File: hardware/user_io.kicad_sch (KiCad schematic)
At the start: 6 parts

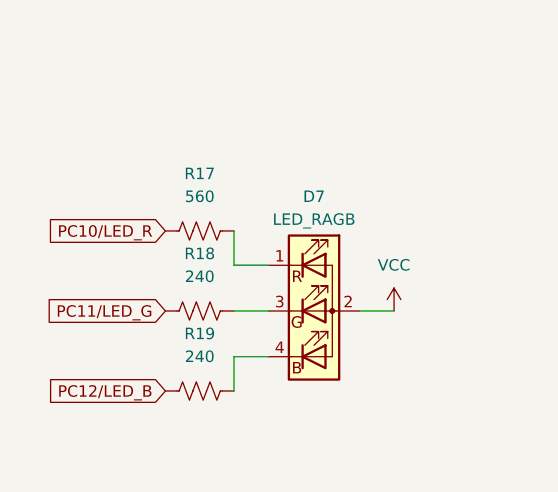
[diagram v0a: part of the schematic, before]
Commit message: wip: schematic fixes based on testing
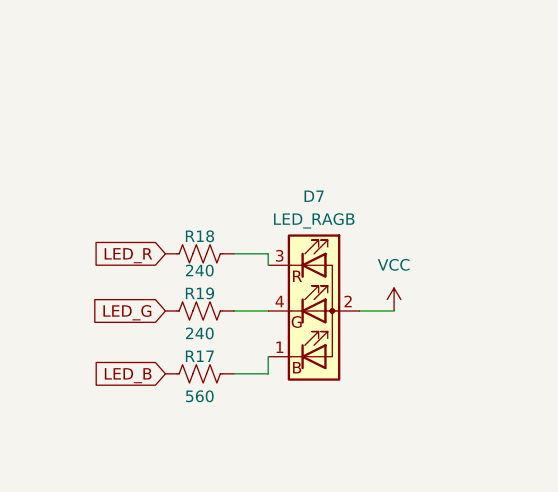
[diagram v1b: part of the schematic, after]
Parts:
- D7: symbol Device:LED_RAGB -> Device:LED_BARG
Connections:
- net PC10/LED_R renamed LED_B
- net PC11/LED_G renamed LED_R
- net PC12/LED_B renamed LED_G
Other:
- moved on the sheet: R17, R18, R19
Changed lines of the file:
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@@
   (title_block
     (title "DSP PAW add-on board")
-    (date "2023-08-19")
+    (date "2023-09-04")
+    (rev "2")
     (company "bitgloo")
     (comment 1 "Released under the CERN Open Hardware Licence Version 2 - Strongly Reciprocal")
   )
+  (wire (pts (xy 96.52 113.665) (xy 100.33 113.665))
+    (stroke (width 0) (type default))
+  )
+  (wire (pts (xy 110.49 106.68) (xy 114.3 106.68))
+    (stroke (width 0) (type default))
+  )
   (wire (pts (xy 96.52 106.68) (xy 100.33 106.68))
     (stroke (width 0) (type default))
   )
-  (wire (pts (xy 96.52 111.76) (xy 100.33 111.76))
-    (stroke (width 0) (type default))
-  )
-  (wire (pts (xy 110.49 106.68) (xy 114.3 106.68))
-    (stroke (width 0) (type default))
-  )
-  (wire (pts (xy 96.52 115.57) (xy 96.52 111.76))
-    (stroke (width 0) (type default))
-  )
-  (wire (pts (xy 96.52 97.79) (xy 96.52 101.6))
-    (stroke (width 0) (type default))
-  )
-  (wire (pts (xy 96.52 101.6) (xy 100.33 101.6))
+  (wire (pts (xy 100.33 113.665) (xy 100.33 111.76))
+    (stroke (width 0) (type default))
+  )
+  (wire (pts (xy 96.52 100.33) (xy 100.33 100.33))
+    (stroke (width 0) (type default))
+  )
+  (wire (pts (xy 100.33 100.33) (xy 100.33 101.6))
     (stroke (width 0) (type default))
   )
@@
     )
   )
-  (global_label "PC12{slash}LED_B" (shape input) (at 88.9 115.57 180) (fields_autoplaced)
+  (global_label "LED_G" (shape input) (at 88.9 106.68 180) (fields_autoplaced)
     (effects (font (size 1.27 1.27)) (justify right))
-    (property "Intersheetrefs" "${INTERSHEET_REFS}" (at 74.5126 115.4906 0)
+    (property "Intersheetrefs" "${INTERSHEET_REFS}" (at 80.3095 106.68 0)
       (effects (font (size 1.27 1.27)) (justify right) hide)
     )
   )
-  (global_label "PC10{slash}LED_R" (shape input) (at 88.9 97.79 180) (fields_autoplaced)
+  (global_label "LED_B" (shape input) (at 88.9 113.665 180) (fields_autoplaced)
     (effects (font (size 1.27 1.27)) (justify right))
-    (property "Intersheetrefs" "${INTERSHEET_REFS}" (at 74.5126 97.7106 0)
+    (property "Intersheetrefs" "${INTERSHEET_REFS}" (at 80.3095 113.665 0)
       (effects (font (size 1.27 1.27)) (justify right) hide)
     )
@@
     )
   )
-  (global_label "PC11{slash}LED_G" (shape input) (at 88.9 106.68 180) (fields_autoplaced)
+  (global_label "LED_R" (shape input) (at 88.9 100.33 180) (fields_autoplaced)
     (effects (font (size 1.27 1.27)) (justify right))
-    (property "Intersheetrefs" "${INTERSHEET_REFS}" (at 74.5126 106.6006 0)
+    (property "Intersheetrefs" "${INTERSHEET_REFS}" (at 80.3095 100.33 0)
       (effects (font (size 1.27 1.27)) (justify right) hide)
     )
@@
     )
   )
-  (symbol (lib_id "Device:R_US") (at 92.71 106.68 90) (unit 1)
-    (in_bom yes) (on_board yes) (dnp no) (fields_autoplaced)
-    (property "Reference" "R18" (at 92.71 100.33 90)
-      (effects (font (size 1.27 1.27)))
-    )
-    (property "Value" "240" (at 92.71 102.87 90)
-      (effects (font (size 1.27 1.27)))
-    )
-    (property "Footprint" "Resistor_SMD:R_0603_1608Metric" (at 92.964 105.664 90)
-      (effects (font (size 1.27 1.27)) hide)
-    )
-    (property "Datasheet" "" (at 92.71 106.68 0)
-      (effects (font (size 1.27 1.27)) hide)
-    )
-    (property "Part Number" "RC0603JR-07240RL" (at 92.71 106.68 0)
-      (effects (font (size 1.27 1.27)) hide)
-    )
-    (property "DNP" "" (at 92.71 106.68 0)
-      (effects (font (size 1.27 1.27)) hide)
-    )
-    (property "LCSC Part #" "C23350" (at 92.71 106.68 0)
+  (symbol (lib_id "Device:R_US") (at 92.71 100.33 90) (unit 1)
+    (in_bom yes) (on_board yes) (dnp no)
+    (property "Reference" "R18" (at 92.71 98.425 90)
+      (effects (font (size 1.27 1.27)))
+    )
+    (property "Value" "240" (at 92.71 102.235 90)
+      (effects (font (size 1.27 1.27)))
+    )
+    (property "Footprint" "Resistor_SMD:R_0603_1608Metric" (at 92.964 99.314 90)
+      (effects (font (size 1.27 1.27)) hide)
+    )
+    (property "Datasheet" "" (at 92.71 100.33 0)
+      (effects (font (size 1.27 1.27)) hide)
+    )
+    (property "Part Number" "RC0603JR-07240RL" (at 92.71 100.33 0)
+      (effects (font (size 1.27 1.27)) hide)
+    )
+    (property "DNP" "" (at 92.71 100.33 0)
+      (effects (font (size 1.27 1.27)) hide)
+    )
+    (property "LCSC Part #" "C23350" (at 92.71 100.33 0)
       (effects (font (size 1.27 1.27)) hide)
     )
@@
     )
   )
-  (symbol (lib_id "Device:R_US") (at 92.71 97.79 90) (unit 1)
-    (in_bom yes) (on_board yes) (dnp no) (fields_autoplaced)
-    (property "Reference" "R17" (at 92.71 91.44 90)
-      (effects (font (size 1.27 1.27)))
-    )
-    (property "Value" "560" (at 92.71 93.98 90)
-      (effects (font (size 1.27 1.27)))
-    )
-    (property "Footprint" "Resistor_SMD:R_0603_1608Metric" (at 92.964 96.774 90)
-      (effects (font (size 1.27 1.27)) hide)
-    )
-    (property "Datasheet" "" (at 92.71 97.79 0)
-      (effects (font (size 1.27 1.27)) hide)
-    )
-    (property "Part Number" "RC0603JR-07560RL" (at 92.71 97.79 0)
-      (effects (font (size 1.27 1.27)) hide)
-    )
-    (property "DNP" "" (at 92.71 97.79 0)
-      (effects (font (size 1.27 1.27)) hide)
-    )
-    (property "LCSC Part #" "C23204" (at 92.71 97.79 0)
+  (symbol (lib_id "Device:R_US") (at 92.71 113.665 90) (unit 1)
+    (in_bom yes) (on_board yes) (dnp no)
+    (property "Reference" "R17" (at 92.71 111.76 90)
+      (effects (font (size 1.27 1.27)))
+    )
+    (property "Value" "560" (at 92.71 116.205 90)
+      (effects (font (size 1.27 1.27)))
+    )
+    (property "Footprint" "Resistor_SMD:R_0603_1608Metric" (at 92.964 112.649 90)
+      (effects (font (size 1.27 1.27)) hide)
+    )
+    (property "Datasheet" "" (at 92.71 113.665 0)
+      (effects (font (size 1.27 1.27)) hide)
+    )
+    (property "Part Number" "RC0603JR-07560RL" (at 92.71 113.665 0)
+      (effects (font (size 1.27 1.27)) hide)
+    )
+    (property "DNP" "" (at 92.71 113.665 0)
+      (effects (font (size 1.27 1.27)) hide)
+    )
+    (property "LCSC Part #" "C23204" (at 92.71 113.665 0)
       (effects (font (size 1.27 1.27)) hide)
     )
@@
     )
   )
-  (symbol (lib_id "Device:LED_RAGB") (at 105.41 106.68 0) (unit 1)
+  (symbol (lib_id "Device:LED_BARG") (at 105.41 106.68 0) (unit 1)
     (in_bom yes) (on_board yes) (dnp no) (fields_autoplaced)
     (property "Reference" "D7" (at 105.41 93.98 0)
@@
     )
   )
-  (symbol (lib_id "Device:R_US") (at 92.71 115.57 90) (unit 1)
-    (in_bom yes) (on_board yes) (dnp no) (fields_autoplaced)
-    (property "Reference" "R19" (at 92.71 109.22 90)
-      (effects (font (size 1.27 1.27)))
-    )
-    (property "Value" "240" (at 92.71 111.76 90)
-      (effects (font (size 1.27 1.27)))
-    )
-    (property "Footprint" "Resistor_SMD:R_0603_1608Metric" (at 92.964 114.554 90)
-      (effects (font (size 1.27 1.27)) hide)
-    )
-    (property "Datasheet" "" (at 92.71 115.57 0)
-      (effects (font (size 1.27 1.27)) hide)
-    )
-    (property "Part Number" "RC0603JR-07240RL" (at 92.71 115.57 0)
-      (effects (font (size 1.27 1.27)) hide)
-    )
-    (property "DNP" "" (at 92.71 115.57 0)
-      (effects (font (size 1.27 1.27)) hide)
-    )
-    (property "LCSC Part #" "C23350" (at 92.71 115.57 0)
-      (effects (font (size 1.27 1.27)) hide)
-    )
+  (symbol (lib_id "Device:R_US") (at 92.71 106.68 90) (unit 1)
+    (in_bom yes) (on_board yes) (dnp no)
+    (property "Reference" "R19" (at 92.71 104.775 90)
+      (effects (font (size 1.27 1.27)))
+    )
+    (property "Value" "240" (at 92.71 109.22 90)
+      (effects (font (size 1.27 1.27)))
+    )
+    (property "Footprint" "Resistor_SMD:R_0603_1608Metric" (at 92.964 105.664 90)
+      (effects (font (size 1.27 1.27)) hide)
+    )
+    (property "Datasheet" "" (at 92.71 106.68 0)
+      (effects (font (size 1.27 1.27)) hide)
+    )
+    (property "Part Number" "RC0603JR-07240RL" (at 92.71 106.68 0)
+      (effects (font (size 1.27 1.27)) hide)
+    )
+    (property "DNP" "" (at 92.71 106.68 0)
+      (effects (font (size 1.27 1.27)) hide)
+    )
+    (property "LCSC Part #" "C23350" (at 92.71 106.68 0)
+      (effects (font (size 1.27 1.27)) hide)
+    )

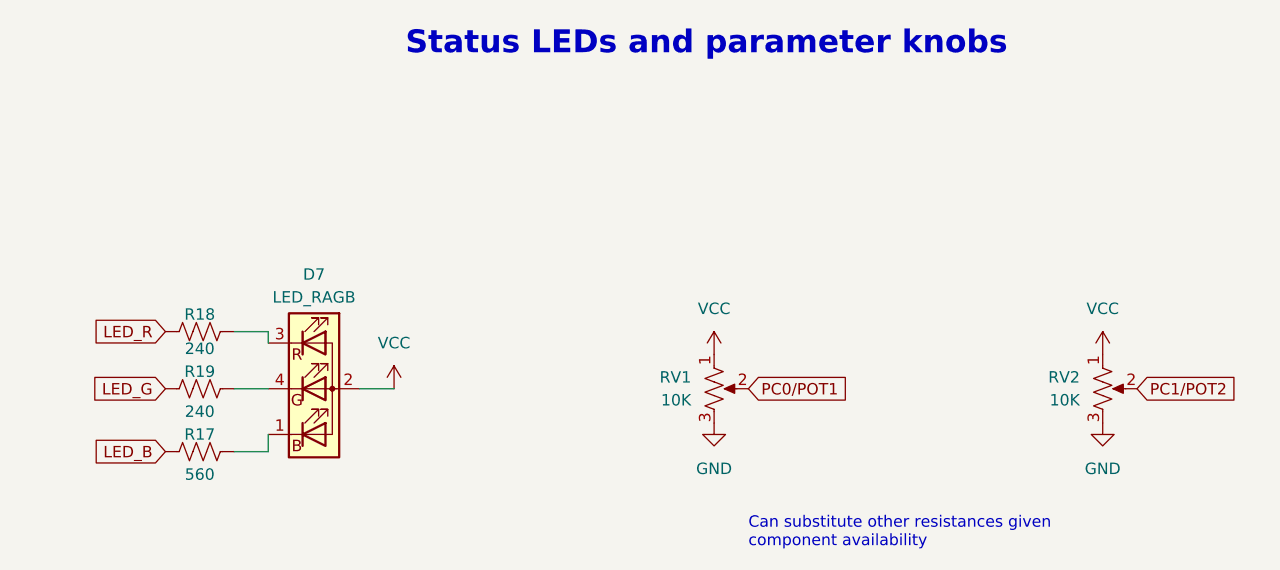
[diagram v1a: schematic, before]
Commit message: vdda buffer; vdda for pots; other fixes
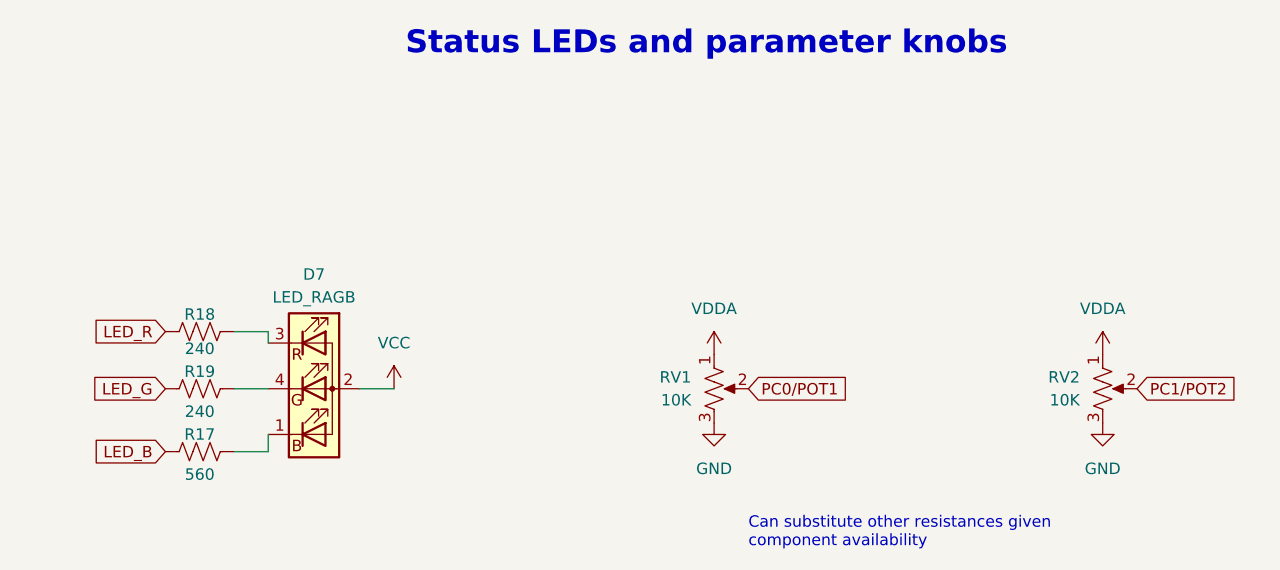
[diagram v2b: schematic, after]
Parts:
- D7: LCSC Part # C427425 -> (none)
- R17: LCSC Part # C23204 -> (none)
- R18, R19: LCSC Part # C23350 -> (none)
- RV1, RV2: LCSC Part # C330458 -> (none)
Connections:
- net VCC: no longer RV1.1, RV2.1
- new net VDDA: RV1.1, RV2.1
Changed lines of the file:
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@@
-      (effects (font (size 1.27 1.27)) hide)
-    )
-    (property "LCSC Part #" "C330458" (at 193.04 106.68 0)
       (effects (font (size 1.27 1.27)) hide)
     )
@@
         (path "/c291319b-d76e-4fda-91cc-061acff65f9f/7798c5d5-f9b1-4b2e-811c-a15abcd34bfa"
           (reference "RV2") (unit 1)
-        )
-      )
-    )
-  )
-  (symbol (lib_id "power:VCC") (at 193.04 102.87 0) (unit 1)
-    (in_bom yes) (on_board yes) (dnp no) (fields_autoplaced)
-    (property "Reference" "#PWR056" (at 193.04 106.68 0)
-      (effects (font (size 1.27 1.27)) hide)
-    )
-    (property "Value" "VCC" (at 193.04 97.79 0)
-      (effects (font (size 1.27 1.27)))
-    )
-    (property "Footprint" "" (at 193.04 102.87 0)
-      (effects (font (size 1.27 1.27)) hide)
-    )
-    (property "Datasheet" "" (at 193.04 102.87 0)
-      (effects (font (size 1.27 1.27)) hide)
-    )
-    (pin "1")
-    (instances
-      (project "stmdsp_rev3"
-        (path "/975c3983-57e7-4e06-a697-831e5209dd80"
-          (reference "#PWR056") (unit 1)
-        )
-      )
-      (project "DSP PAW add-on board"
-        (path "/c291319b-d76e-4fda-91cc-061acff65f9f/270d19d2-3af2-41db-ad1c-33373417ec82"
-          (reference "#PWR027") (unit 1)
-        )
-        (path "/c291319b-d76e-4fda-91cc-061acff65f9f/7798c5d5-f9b1-4b2e-811c-a15abcd34bfa"
-          (reference "#PWR068") (unit 1)
         )
       )
@@
       (effects (font (size 1.27 1.27)) hide)
     )
-    (property "LCSC Part #" "C23350" (at 92.71 100.33 0)
-      (effects (font (size 1.27 1.27)) hide)
-    )
     (pin "1")
     (pin "2")
@@
         (path "/c291319b-d76e-4fda-91cc-061acff65f9f/7798c5d5-f9b1-4b2e-811c-a15abcd34bfa"
           (reference "#PWR070") (unit 1)
+        )
+      )
+    )
+  )
+  (symbol (lib_id "power:VDDA") (at 193.04 102.87 0) (unit 1)
+    (in_bom yes) (on_board yes) (dnp no) (fields_autoplaced)
+    (property "Reference" "#PWR013" (at 193.04 106.68 0)
+      (effects (font (size 1.27 1.27)) hide)
+    )
+    (property "Value" "VDDA" (at 193.04 97.79 0)
+      (effects (font (size 1.27 1.27)))
+    )
+    (property "Footprint" "" (at 193.04 102.87 0)
+      (effects (font (size 1.27 1.27)) hide)
+    )
+    (property "Datasheet" "" (at 193.04 102.87 0)
+      (effects (font (size 1.27 1.27)) hide)
+    )
+    (pin "1")
+    (instances
+      (project "stmdsp_rev3"
+        (path "/975c3983-57e7-4e06-a697-831e5209dd80"
+          (reference "#PWR013") (unit 1)
+        )
+      )
+      (project "DSP PAW add-on board"
+        (path "/c291319b-d76e-4fda-91cc-061acff65f9f/270d19d2-3af2-41db-ad1c-33373417ec82"
+          (reference "#PWR033") (unit 1)
+        )
+        (path "/c291319b-d76e-4fda-91cc-061acff65f9f/97fc232a-dbc7-49da-a6a0-e33e9aacbabd"
+          (reference "#PWR024") (unit 1)
+        )
+        (path "/c291319b-d76e-4fda-91cc-061acff65f9f/7798c5d5-f9b1-4b2e-811c-a15abcd34bfa"
+          (reference "#PWR067") (unit 1)
         )
       )
@@
       (effects (font (size 1.27 1.27)) hide)
     )
-    (property "LCSC Part #" "C23204" (at 92.71 113.665 0)
-      (effects (font (size 1.27 1.27)) hide)
-    )
     (pin "1")
     (pin "2")
@@
     )
   )
-  (symbol (lib_id "power:VCC") (at 149.86 102.87 0) (unit 1)
-    (in_bom yes) (on_board yes) (dnp no) (fields_autoplaced)
-    (property "Reference" "#PWR055" (at 149.86 106.68 0)
-      (effects (font (size 1.27 1.27)) hide)
-    )
-    (property "Value" "VCC" (at 149.86 97.79 0)
-      (effects (font (size 1.27 1.27)))
-    )
-    (property "Footprint" "" (at 149.86 102.87 0)
-      (effects (font (size 1.27 1.27)) hide)
-    )
-    (property "Datasheet" "" (at 149.86 102.87 0)
-      (effects (font (size 1.27 1.27)) hide)
-    )
-    (pin "1")
-    (instances
-      (project "stmdsp_rev3"
-        (path "/975c3983-57e7-4e06-a697-831e5209dd80"
-          (reference "#PWR055") (unit 1)
-        )
-      )
-      (project "DSP PAW add-on board"
-        (path "/c291319b-d76e-4fda-91cc-061acff65f9f/270d19d2-3af2-41db-ad1c-33373417ec82"
-          (reference "#PWR023") (unit 1)
-        )
-        (path "/c291319b-d76e-4fda-91cc-061acff65f9f/7798c5d5-f9b1-4b2e-811c-a15abcd34bfa"
-          (reference "#PWR067") (unit 1)
-        )
-      )
-    )
-  )
   (symbol (lib_id "Device:LED_BARG") (at 105.41 106.68 0) (unit 1)
     (in_bom yes) (on_board yes) (dnp no) (fields_autoplaced)
@@
     )
     (property "DNP" "" (at 105.41 106.68 0)
-      (effects (font (size 1.27 1.27)) hide)
-    )
-    (property "LCSC Part #" "C427425" (at 105.41 106.68 0)
       (effects (font (size 1.27 1.27)) hide)
     )
@@
       (effects (font (size 1.27 1.27)) hide)
     )
-    (property "LCSC Part #" "C23350" (at 92.71 106.68 0)
-      (effects (font (size 1.27 1.27)) hide)
-    )
     (pin "1")
     (pin "2")
@@
         (path "/c291319b-d76e-4fda-91cc-061acff65f9f/7798c5d5-f9b1-4b2e-811c-a15abcd34bfa"
           (reference "R25") (unit 1)
+        )
+      )
+    )
+  )
+  (symbol (lib_id "power:VDDA") (at 149.86 102.87 0) (unit 1)
+    (in_bom yes) (on_board yes) (dnp no) (fields_autoplaced)
+    (property "Reference" "#PWR013" (at 149.86 106.68 0)
+      (effects (font (size 1.27 1.27)) hide)
+    )
+    (property "Value" "VDDA" (at 149.86 97.79 0)
+      (effects (font (size 1.27 1.27)))
+    )
+    (property "Footprint" "" (at 149.86 102.87 0)
+      (effects (font (size 1.27 1.27)) hide)
+    )
+    (property "Datasheet" "" (at 149.86 102.87 0)
+      (effects (font (size 1.27 1.27)) hide)
+    )
+    (pin "1")
+    (instances
+      (project "stmdsp_rev3"
+        (path "/975c3983-57e7-4e06-a697-831e5209dd80"
+          (reference "#PWR013") (unit 1)
+        )
+      )
+      (project "DSP PAW add-on board"
+        (path "/c291319b-d76e-4fda-91cc-061acff65f9f/270d19d2-3af2-41db-ad1c-33373417ec82"
+          (reference "#PWR033") (unit 1)
+        )
+        (path "/c291319b-d76e-4fda-91cc-061acff65f9f/97fc232a-dbc7-49da-a6a0-e33e9aacbabd"
+          (reference "#PWR024") (unit 1)
+        )
+        (path "/c291319b-d76e-4fda-91cc-061acff65f9f/7798c5d5-f9b1-4b2e-811c-a15abcd34bfa"
+          (reference "#PWR054") (unit 1)
         )
       )
@@
       (effects (font (size 1.27 1.27)) hide)
     )
-    (property "LCSC Part #" "C330458" (at 149.86 106.68 0)
-      (effects (font (size 1.27 1.27)) hide)
-    )
